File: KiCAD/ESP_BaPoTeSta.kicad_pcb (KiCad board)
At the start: 2 copper layers, 39.4 x 49.5 mm, 32 parts, among them P1 Progr, P10 CONN_01X04, P13 CONN_01X03, P15 CONN_01X04, P2 Battery, P4 Upload, P5 Config, P9 CONN_01X04, Q1 IRLML6302, U1 MCP1700-330, U2 ESP-12

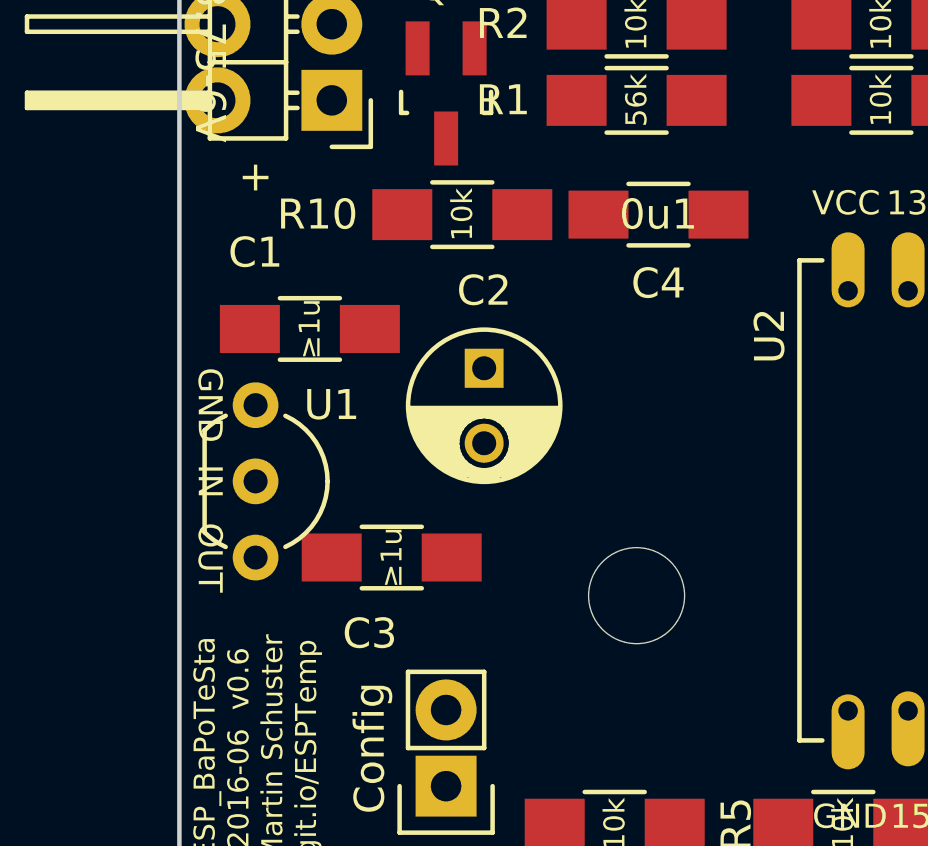
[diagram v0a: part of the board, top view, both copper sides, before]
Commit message: ENH: PCB: use SOT-23 MCP1700
takes less space, easier to solder
obsoletes #21
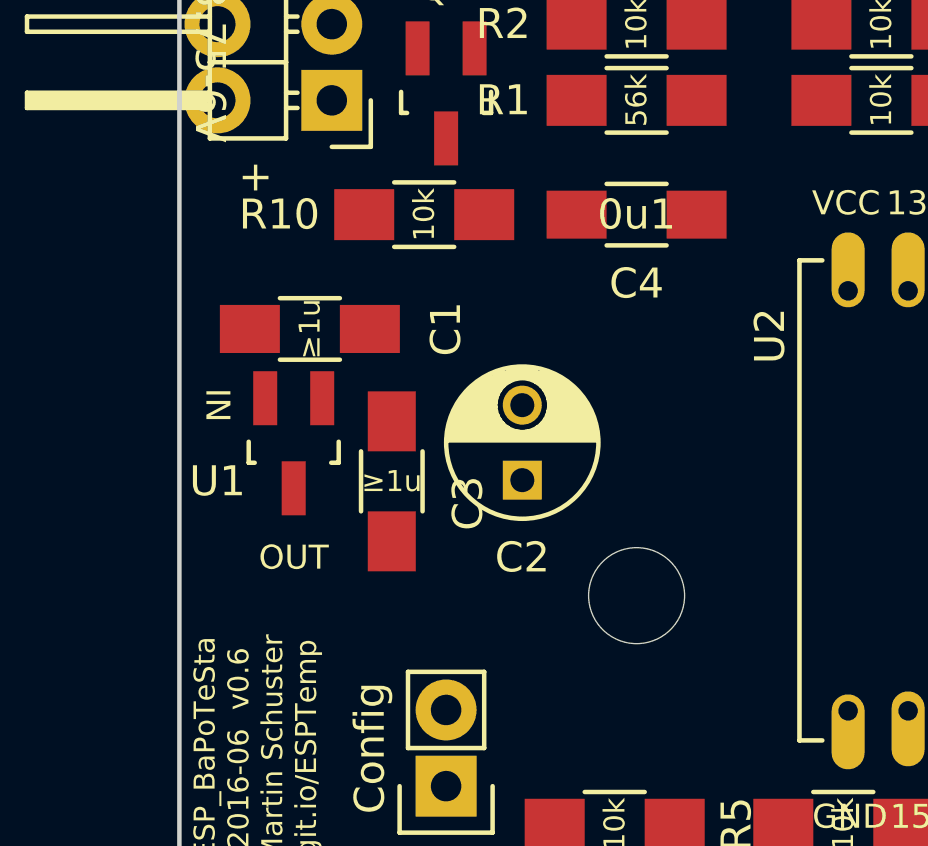
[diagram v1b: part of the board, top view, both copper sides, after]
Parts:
- U1: footprint TO_SOT_Packages_THT:TO-92_Inline_Wide -> TO_SOT_Packages_SMD:SOT-23_Handsoldering
- moved C2 3.94 mm to (134.6, 97.8), turned to 90 degrees
- moved C3 2.54 mm to (130.3, 97.8), turned to 90 degrees
- moved U1 1.80 mm to (127.0, 96.5), turned to 180 degrees
- moved R10 1.27 mm to (131.3, 88.9)
- moved C4 0.73 mm to (138.4, 88.9)
- turned C1 to 0 degrees
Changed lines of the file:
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@@
 (kicad_pcb (version 4) (host pcbnew 4.0.2+dfsg1-2~bpo8+1-stable)
   (general
-    (links 0)
+    (links 61)
     (no_connects 47)
     (area 123.114999 65.964999 162.635001 115.645001)
     (thickness 1.6)
-    (drawings 79)
+    (drawings 78)
     (tracks 1)
     (zones 0)
@@
   )
   (module Resistors_SMD:R_1206_HandSoldering (layer F.Cu)
-    (at 132.62 88.9)
+    (at 131.35 88.9)
     (descr "Resistor SMD 1206, hand soldering")
     (tags "resistor 1206")
@@
   )
   (module Capacitors_SMD:C_1206_HandSoldering (layer F.Cu)
-    (at 127.54 92.71 180)
+    (at 127.54 92.71)
     (descr "Capacitor SMD 1206, hand soldering")
     (tags "capacitor 1206")
     (attr smd)
-    (fp_text reference C1 (at 1.81 2.54 180) (layer F.SilkS)
-      (effects (font (size 1 1) (thickness 0.15)))
-    )
-    (fp_text value ≥1u (at 0 0 270) (layer F.SilkS)
-      (effects (font (size 0.7 0.7) (thickness 0.1)))
-    )
-    (fp_line (start -3.3 -1.15) (end 3.3 -1.15) (layer F.CrtYd) (width 0.05))
-    (fp_line (start -3.3 1.15) (end 3.3 1.15) (layer F.CrtYd) (width 0.05))
-    (fp_line (start -3.3 -1.15) (end -3.3 1.15) (layer F.CrtYd) (width 0.05))
-    (fp_line (start 3.3 -1.15) (end 3.3 1.15) (layer F.CrtYd) (width 0.05))
-    (fp_line (start 1 -1.025) (end -1 -1.025) (layer F.SilkS) (width 0.15))
-    (fp_line (start -1 1.025) (end 1 1.025) (layer F.SilkS) (width 0.15))
-    (pad 1 smd rect (at -2 0 180) (size 2 1.6) (layers F.Cu F.Paste F.Mask)
-      (net 1 +BATT))
-    (pad 2 smd rect (at 2 0 180) (size 2 1.6) (layers F.Cu F.Paste F.Mask)
-      (net 2 GND))
-    (model Capacitors_SMD.3dshapes/C_1206_HandSoldering.wrl
-      (at (xyz 0 0 0))
-      (scale (xyz 1 1 1))
-      (rotate (xyz 0 0 0))
-    )
-  )
-  (module Capacitors_SMD:C_1206_HandSoldering (layer F.Cu)
-    (at 130.27 100.33)
-    (descr "Capacitor SMD 1206, hand soldering")
-    (tags "capacitor 1206")
-    (attr smd)
-    (fp_text reference C3 (at -0.73 2.54) (layer F.SilkS)
+    (fp_text reference C1 (at 4.54 0 90) (layer F.SilkS)
       (effects (font (size 1 1) (thickness 0.15)))
     )
@@
     (fp_line (start -1 1.025) (end 1 1.025) (layer F.SilkS) (width 0.15))
     (pad 1 smd rect (at -2 0) (size 2 1.6) (layers F.Cu F.Paste F.Mask)
+      (net 1 +BATT))
+    (pad 2 smd rect (at 2 0) (size 2 1.6) (layers F.Cu F.Paste F.Mask)
+      (net 2 GND))
+    (model Capacitors_SMD.3dshapes/C_1206_HandSoldering.wrl
+      (at (xyz 0 0 0))
+      (scale (xyz 1 1 1))
+      (rotate (xyz 0 0 0))
+    )
+  )
+  (module Capacitors_SMD:C_1206_HandSoldering (layer F.Cu)
+    (at 130.27 97.79 90)
+    (descr "Capacitor SMD 1206, hand soldering")
+    (tags "capacitor 1206")
+    (attr smd)
+    (fp_text reference C3 (at -0.73 2.54 90) (layer F.SilkS)
+      (effects (font (size 1 1) (thickness 0.15)))
+    )
+    (fp_text value ≥1u (at 0 0 180) (layer F.SilkS)
+      (effects (font (size 0.7 0.7) (thickness 0.1)))
+    )
+    (fp_line (start -3.3 -1.15) (end 3.3 -1.15) (layer F.CrtYd) (width 0.05))
+    (fp_line (start -3.3 1.15) (end 3.3 1.15) (layer F.CrtYd) (width 0.05))
+    (fp_line (start -3.3 -1.15) (end -3.3 1.15) (layer F.CrtYd) (width 0.05))
+    (fp_line (start 3.3 -1.15) (end 3.3 1.15) (layer F.CrtYd) (width 0.05))
+    (fp_line (start 1 -1.025) (end -1 -1.025) (layer F.SilkS) (width 0.15))
+    (fp_line (start -1 1.025) (end 1 1.025) (layer F.SilkS) (width 0.15))
+    (pad 1 smd rect (at -2 0 90) (size 2 1.6) (layers F.Cu F.Paste F.Mask)
       (net 3 VCC))
-    (pad 2 smd rect (at 2 0) (size 2 1.6) (layers F.Cu F.Paste F.Mask)
+    (pad 2 smd rect (at 2 0 90) (size 2 1.6) (layers F.Cu F.Paste F.Mask)
       (net 2 GND))
     (model Capacitors_SMD.3dshapes/C_1206_HandSoldering.wrl
@@
   )
   (module Capacitors_ThroughHole:C_Radial_D5_L11_P2.5 (layer F.Cu)
-    (at 133.35 94.02 270)
+    (at 134.62 97.75 90)
     (descr "Radial Electrolytic Capacitor Diameter 5mm x Length 11mm, Pitch 2.5mm")
     (tags "Electrolytic Capacitor")
-    (fp_text reference C2 (at -2.58 0 360) (layer F.SilkS)
-      (effects (font (size 1 1) (thickness 0.15)))
-    )
-    (fp_text value ≥10u (at 1.25 3.8 270) (layer F.Fab) hide
+    (fp_text reference C2 (at -2.58 0 180) (layer F.SilkS)
+      (effects (font (size 1 1) (thickness 0.15)))
+    )
+    (fp_text value ≥10u (at 1.25 3.8 90) (layer F.Fab) hide
       (effects (font (size 1 1) (thickness 0.15)))
     )
@@
     (fp_circle (center 1.25 0) (end 1.25 -2.5375) (layer F.SilkS) (width 0.15))
     (fp_circle (center 1.25 0) (end 1.25 -2.8) (layer F.CrtYd) (width 0.05))
-    (pad 1 thru_hole rect (at 0 0 270) (size 1.3 1.3) (drill 0.8) (layers *.Cu *.Mask F.SilkS)
+    (pad 1 thru_hole rect (at 0 0 90) (size 1.3 1.3) (drill 0.8) (layers *.Cu *.Mask F.SilkS)
       (net 3 VCC))
-    (pad 2 thru_hole circle (at 2.5 0 270) (size 1.3 1.3) (drill 0.8) (layers *.Cu *.Mask F.SilkS)
+    (pad 2 thru_hole circle (at 2.5 0 90) (size 1.3 1.3) (drill 0.8) (layers *.Cu *.Mask F.SilkS)
       (net 2 GND))
     (model Capacitors_ThroughHole.3dshapes/C_Radial_D5_L11_P2.5.wrl
@@
     )
   )
-  (module TO_SOT_Packages_THT:TO-92_Inline_Wide (layer F.Cu)
-    (at 125.73 95.25 270)
-    (descr "TO-92 leads in-line, wide, drill 0.8mm (see NXP sot054_po.pdf)")
-    (tags "to-92 sc-43 sc-43a sot54 PA33 transistor")
-    (fp_text reference U1 (at 0 -2.54 540) (layer F.SilkS)
-      (effects (font (size 1 1) (thickness 0.15)))
-    )
-    (fp_text value MCP1700-330 (at 0 3 270) (layer F.Fab) hide
-      (effects (font (size 1 1) (thickness 0.15)))
-    )
-    (fp_arc (start 2.54 0) (end 0.84 1.7) (angle 20.5) (layer F.SilkS) (width 0.15))
-    (fp_arc (start 2.54 0) (end 4.24 1.7) (angle -20.5) (layer F.SilkS) (width 0.15))
-    (fp_line (start -1 1.95) (end -1 -2.65) (layer F.CrtYd) (width 0.05))
-    (fp_line (start -1 1.95) (end 6.1 1.95) (layer F.CrtYd) (width 0.05))
-    (fp_line (start 0.84 1.7) (end 4.24 1.7) (layer F.SilkS) (width 0.15))
-    (fp_arc (start 2.54 0) (end 2.54 -2.4) (angle -65.55604127) (layer F.SilkS) (width 0.15))
-    (fp_arc (start 2.54 0) (end 2.54 -2.4) (angle 65.55604127) (layer F.SilkS) (width 0.15))
-    (fp_line (start -1 -2.65) (end 6.1 -2.65) (layer F.CrtYd) (width 0.05))
-    (fp_line (start 6.1 1.95) (end 6.1 -2.65) (layer F.CrtYd) (width 0.05))
-    (pad 2 thru_hole circle (at 2.54 0) (size 1.524 1.524) (drill 0.8) (layers *.Cu *.Mask F.SilkS)
-      (net 1 +BATT))
-    (pad 3 thru_hole circle (at 5.08 0) (size 1.524 1.524) (drill 0.8) (layers *.Cu *.Mask F.SilkS)
-      (net 3 VCC))
-    (pad 1 thru_hole circle (at 0 0) (size 1.524 1.524) (drill 0.8) (layers *.Cu *.Mask F.SilkS)
-      (net 2 GND))
-    (model TO_SOT_Packages_THT.3dshapes/TO-92_Inline_Wide.wrl
-      (at (xyz 0.1 0 0))
-      (scale (xyz 1 1 1))
-      (rotate (xyz 0 0 -90))
-    )
-  )
   (module Capacitors_SMD:C_1206_HandSoldering (layer F.Cu)
-    (at 139.16 88.9 180)
+    (at 138.43 88.9 180)
     (descr "Capacitor SMD 1206, hand soldering")
     (tags "capacitor 1206")
@@
     (pad 1 np_thru_hole circle (at 0 0) (size 3.2 3.2) (drill 3.2) (layers *.Cu *.Mask F.SilkS))
   )
+  (module TO_SOT_Packages_SMD:SOT-23_Handsoldering (layer F.Cu)
+    (at 127 96.52 180)
+    (descr "SOT-23, Handsoldering")
+    (tags SOT-23)
+    (attr smd)
+    (fp_text reference U1 (at 2.54 -1.27 180) (layer F.SilkS)
+      (effects (font (size 1 1) (thickness 0.15)))
+    )
+    (fp_text value MCP1700-330 (at 0 3.81 180) (layer F.Fab) hide
+      (effects (font (size 1 1) (thickness 0.15)))
+    )
+    (fp_line (start -1.49982 0.0508) (end -1.49982 -0.65024) (layer F.SilkS) (width 0.15))
+    (fp_line (start -1.49982 -0.65024) (end -1.2509 -0.65024) (layer F.SilkS) (width 0.15))
+    (fp_line (start 1.29916 -0.65024) (end 1.49982 -0.65024) (layer F.SilkS) (width 0.15))
+    (fp_line (start 1.49982 -0.65024) (end 1.49982 0.0508) (layer F.SilkS) (width 0.15))
+    (pad 1 smd rect (at -0.95 1.50114 180) (size 0.8001 1.80086) (layers F.Cu F.Paste F.Mask)
+      (net 2 GND))
+    (pad 2 smd rect (at 0.95 1.50114 180) (size 0.8001 1.80086) (layers F.Cu F.Paste F.Mask)
+      (net 1 +BATT))
+    (pad 3 smd rect (at 0 -1.50114 180) (size 0.8001 1.80086) (layers F.Cu F.Paste F.Mask)
+      (net 3 VCC))
+    (model TO_SOT_Packages_SMD.3dshapes/SOT-23_Handsoldering.wrl
+      (at (xyz 0 0 0))
+      (scale (xyz 1 1 1))
+      (rotate (xyz 0 0 0))
+    )
+  )
   (gr_line (start 137.16 76.2) (end 138.43 76.2) (layer F.SilkS) (width 0.2))
   (gr_line (start 137.16 73.66) (end 138.43 73.66) (layer F.SilkS) (width 0.2))
@@
     (effects (font (size 1 1) (thickness 0.15)) (justify mirror))
   )
-  (gr_text GND (at 124.206 95.25 270) (layer F.SilkS)
-    (effects (font (size 0.8 0.8) (thickness 0.15)))
-  )
   (gr_text RST (at 159.512 93.472) (layer B.SilkS)
     (effects (font (size 0.6 0.6) (thickness 0.12)) (justify mirror))
@@
     (effects (font (size 0.8 0.8) (thickness 0.16)))
   )
-  (gr_text OUT (at 124.206 100.33 270) (layer F.SilkS)
+  (gr_text OUT (at 127 100.33 360) (layer F.SilkS)
     (effects (font (size 0.8 0.8) (thickness 0.15)))
   )
-  (gr_text IN (at 124.206 97.79 270) (layer F.SilkS)
+  (gr_text IN (at 124.46 95.25 270) (layer F.SilkS)
     (effects (font (size 0.8 0.8) (thickness 0.15)))
   )

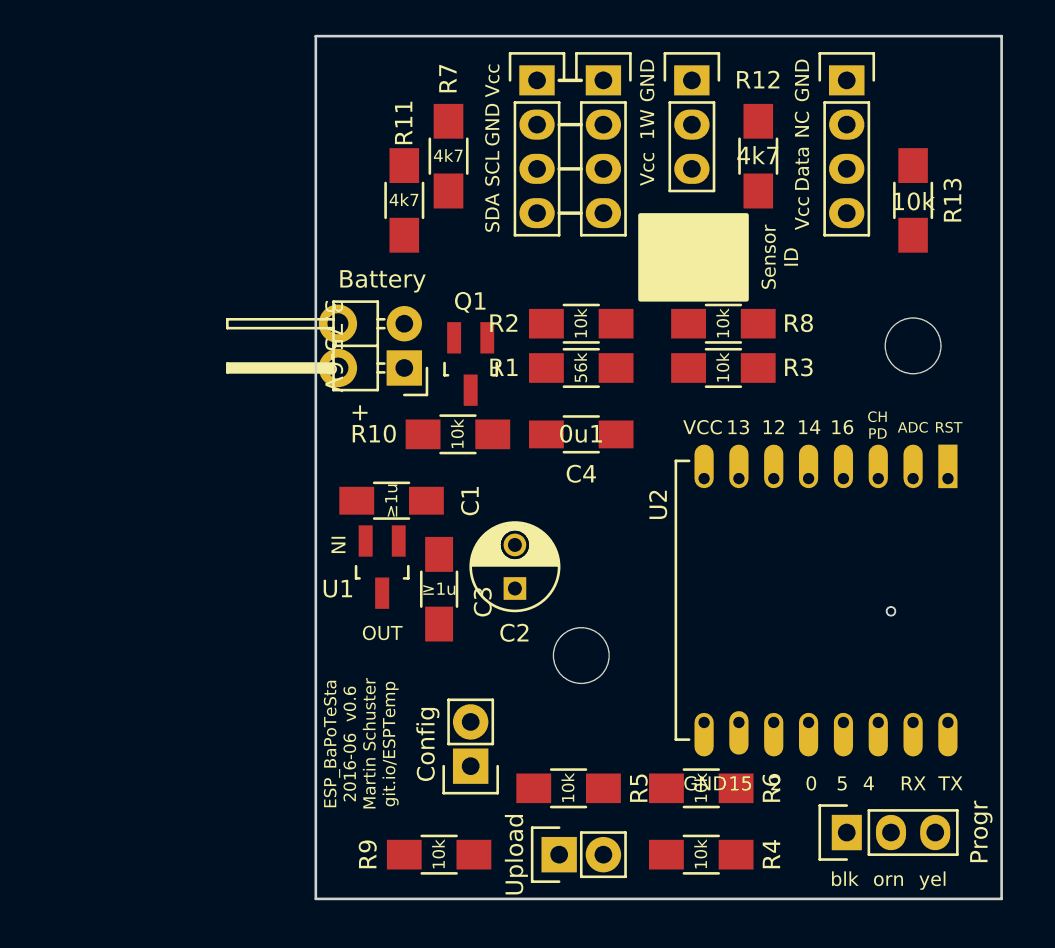
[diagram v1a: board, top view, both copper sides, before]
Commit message: ENH: PCB: minor cosmetical changes
move left mounting hole
move el.cap
lines for pin labels at headers
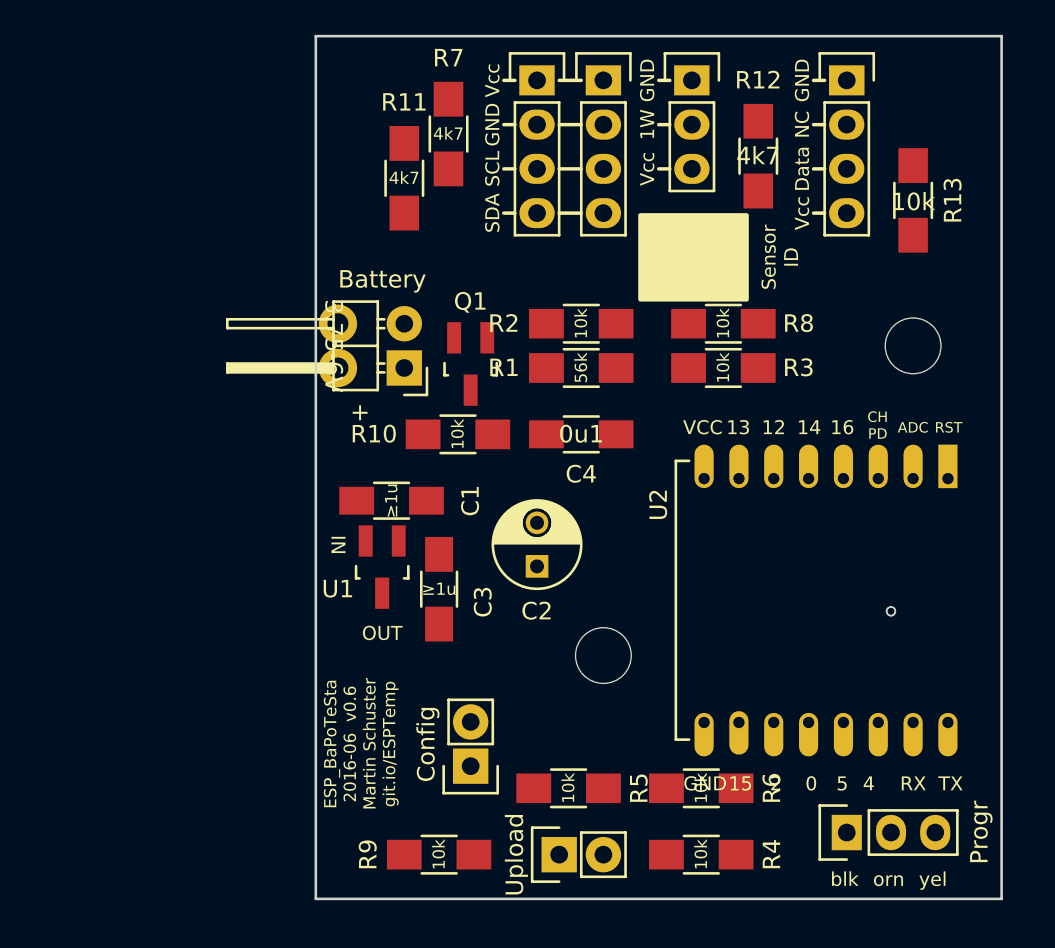
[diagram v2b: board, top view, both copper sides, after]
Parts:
- moved C2 1.80 mm to (135.9, 96.5)
- moved R7 1.27 mm to (130.8, 71.7)
- moved R11 1.27 mm to (128.3, 74.2)
- moved REF** 1.27 mm to (139.7, 101.6)
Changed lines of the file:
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@@
     (area 123.114999 65.964999 162.635001 115.645001)
     (thickness 1.6)
-    (drawings 78)
+    (drawings 89)
     (tracks 1)
     (zones 0)
@@
   )
   (module Mounting_Holes:MountingHole_3.2mm_M3_ISO7380 (layer F.Cu)
-    (at 138.43 101.6)
+    (at 139.7 101.6)
     (descr "Mounting Hole 3.2mm, no annular, M3, ISO7380")
     (tags "mounting hole 3.2mm no annular m3 iso7380")
@@
   )
   (module Resistors_SMD:R_1206_HandSoldering (layer F.Cu)
-    (at 130.81 72.93 90)
+    (at 130.81 71.66 90)
     (descr "Resistor SMD 1206, hand soldering")
     (tags "resistor 1206")
     (attr smd)
-    (fp_text reference R7 (at 4.445 0 90) (layer F.SilkS)
+    (fp_text reference R7 (at 4.35 0 180) (layer F.SilkS)
       (effects (font (size 1 1) (thickness 0.15)))
     )
@@
   )
   (module Resistors_SMD:R_1206_HandSoldering (layer F.Cu)
-    (at 128.27 75.47 90)
+    (at 128.27 74.2 90)
     (descr "Resistor SMD 1206, hand soldering")
     (tags "resistor 1206")
     (attr smd)
-    (fp_text reference R11 (at 4.445 0 90) (layer F.SilkS)
+    (fp_text reference R11 (at 4.35 0 180) (layer F.SilkS)
       (effects (font (size 1 1) (thickness 0.15)))
     )
@@
   )
   (module Capacitors_ThroughHole:C_Radial_D5_L11_P2.5 (layer F.Cu)
-    (at 134.62 97.75 90)
+    (at 135.89 96.48 90)
     (descr "Radial Electrolytic Capacitor Diameter 5mm x Length 11mm, Pitch 2.5mm")
     (tags "Electrolytic Capacitor")
@@
     )
   )
+  (gr_line (start 152.4 68.58) (end 151.765 68.58) (layer F.SilkS) (width 0.2))
+  (gr_line (start 152.4 71.12) (end 151.765 71.12) (layer F.SilkS) (width 0.2))
+  (gr_line (start 152.4 73.66) (end 151.765 73.66) (layer F.SilkS) (width 0.2))
+  (gr_line (start 152.4 76.2) (end 151.765 76.2) (layer F.SilkS) (width 0.2))
+  (gr_line (start 143.51 68.58) (end 142.875 68.58) (layer F.SilkS) (width 0.2))
+  (gr_line (start 143.51 71.12) (end 142.875 71.12) (layer F.SilkS) (width 0.2))
+  (gr_line (start 143.51 73.66) (end 142.875 73.66) (layer F.SilkS) (width 0.2))
+  (gr_line (start 134.62 68.58) (end 133.985 68.58) (layer F.SilkS) (width 0.2))
+  (gr_line (start 134.62 71.12) (end 133.985 71.12) (layer F.SilkS) (width 0.2))
+  (gr_line (start 134.62 73.66) (end 133.985 73.66) (layer F.SilkS) (width 0.2))
+  (gr_line (start 134.62 76.2) (end 133.985 76.2) (layer F.SilkS) (width 0.2))
   (gr_line (start 137.16 76.2) (end 138.43 76.2) (layer F.SilkS) (width 0.2))
   (gr_line (start 137.16 73.66) (end 138.43 73.66) (layer F.SilkS) (width 0.2))
@@
     (effects (font (size 0.8 0.8) (thickness 0.16)))
   )
-  (gr_text OUT (at 127 100.33 360) (layer F.SilkS)
+  (gr_text OUT (at 127 100.33) (layer F.SilkS)
     (effects (font (size 0.8 0.8) (thickness 0.15)))
   )

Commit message: WIP: PCB: started routing sensors
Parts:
- moved R13 9.98 mm to (148.6, 80.0), turned to 180 degrees
- moved C4 5.08 mm to (138.4, 83.8)
- moved R1 3.81 mm to (138.4, 88.9)
- moved R2 3.81 mm to (138.4, 86.4)
- moved R3 3.23 mm to (148.6, 82.5)
- moved R8 3.23 mm to (148.6, 85.1)
- moved R7 2.64 mm to (128.3, 72.4)
- moved R11 2.54 mm to (130.8, 74.2)
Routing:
- net PwrSens: track 0.00 -> 59.9 mm, vias 0 -> 2
- net DHTData: track 0.00 -> 55.6 mm, vias 0 -> 3
- net 1Wire: track 0.00 -> 40.5 mm, vias 0 -> 3
- net SCL: track 0.00 -> 40.2 mm, vias 0 -> 2
- net VCC: track 0.00 -> 23.6 mm
- net ADC: track 0.00 -> 22.0 mm, vias 0 -> 1
- net SDA: track 0.00 -> 20.3 mm, vias 0 -> 1
- net /RST: track 0.00 -> 16.4 mm
- net /CH_PD: track 0.00 -> 11.8 mm

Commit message: WIP: PCB: continued routing
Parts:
- moved C3 9.80 mm to (126.7, 88.6), turned to 180 degrees
- moved R10 7.88 mm to (133.3, 81.3)
- moved U1 4.34 mm to (128.6, 92.5), turned to 0 degrees
- moved C1 3.88 mm to (128.3, 96.5), turned to 180 degrees
- moved R9 3.12 mm to (132.1, 110.5), turned to 90 degrees
- moved P5 2.54 mm to (132.1, 105.4), turned to 90 degrees
- moved R4 2.00 mm to (147.3, 113.0)
- moved R6 1.46 mm to (146.1, 110.5)
- moved Q1 1.29 mm to (133.3, 85.1)
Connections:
- P2 pad 1: +BATT -> GND
- P2 pad 2: GND -> +BATT
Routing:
- net GND: track 0.00 -> 55.0 mm, vias 0 -> 2
- net VCC: track 23.6 -> 49.4 mm, vias 0 -> 1
- net +BATT: track 0.00 -> 23.1 mm
- net /GPIO0: track 0.00 -> 9.36 mm
- net SDA: track 20.3 -> 29.2 mm
- net Net-(P1-Pad2): track 0.00 -> 6.85 mm
- net Net-(P1-Pad3): track 0.00 -> 6.62 mm
- net /G: track 0.00 -> 5.73 mm
- net /GPIO15: track 0.00 -> 5.29 mm
- net Net-(Q1-Pad3): track 0.00 -> 4.33 mm
- net 1Wire: track 40.5 -> 44.4 mm
- net SCL: track 40.2 -> 44.0 mm
- net /GPIO4: track 0.00 -> 3.08 mm
- net (no net): vias 1 -> 0
